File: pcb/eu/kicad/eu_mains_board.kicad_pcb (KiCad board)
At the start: 2 copper layers, 57.9 x 57.9 mm, 10 parts, among them J1 2604-3102, J2 2604-3102, J3 TSM-102-01-L-SV

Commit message: Boards for v0.4: ring board, mic carrier, riser, cover flex, EU cap board, wiring board posts
- Ring board, mic carrier and riser in pcb/sensor/ (D-50, D-60, D-68); carrier and riser fab
  packs; the ring board waits on the MSR-2's CN2 part and map
- Riser 14 x 12 mm, pins above and between the posts; cover flex with the run past the GND
  contact post and a jog from the pad section (D-79)
- EU cap board on the carrier, closed snap windows, wider with the face plate (D-56, D-70,
  D-77, D-78); EU 5 V board pins follow the back cover's pads
- Wiring board: WA-SMSI spacer posts in the 5 V area (SMT, spigot inside the board), J2
- ERC / DRC clean on every board
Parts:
- J3: value TSM-102-01-L-SV -> TSM-102-02-L-SV
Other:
- board text added: "J3 Samtec TSM-102-02-L-SV"
- board text removed: "J3 Samtec TSM-102-01-L-SV"

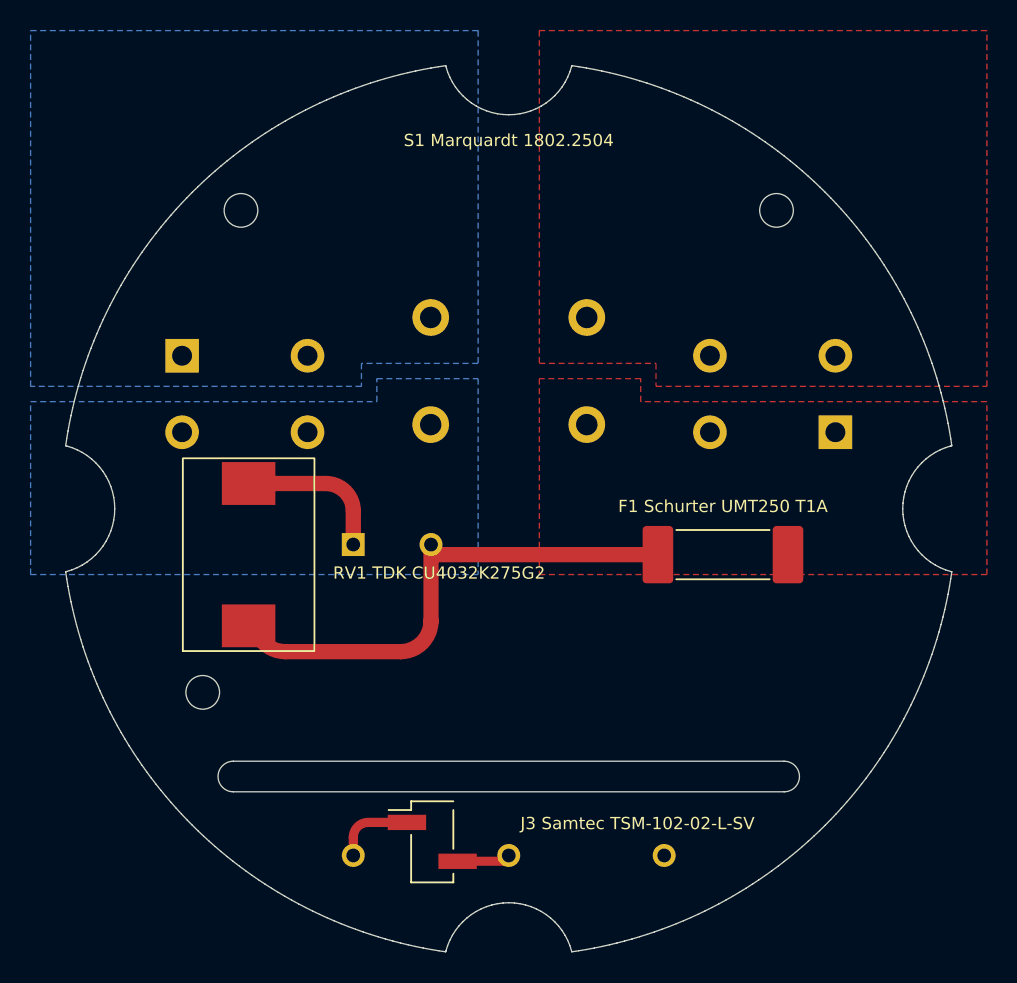
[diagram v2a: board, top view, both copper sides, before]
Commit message: Mic on the boards, parts audit, rocker second source, CN2 land pattern, back cover fit (D-82..D-90)
- Prototype PCBWay packs for the ring board, EU cap board and cover flex; logos and URL on the
  boards with room for them
- CN2 mate: Molex 55909-2474 on an assumed 51338-2474 (D-82); land pattern from Molex
  SD-55909-003 rev J, B2B from SD-51338-003 rev K (D-89); contact map and pin 1 still open
- Microphone: Knowles SPK0641HT4H-1 + ADAU7002 on the ring board and the EU cap board, the mic
  carrier removed; face plate sound column on a gasket (D-83); C3 KEMET C1206C104J3GACTU C0G
  (D-85)
- Parts rule (active, stocked at DigiKey or Mouser) and audit: F1 3403.0166.11, cover flex 1 uF
  CL05A105KO5NNNC, rocker at Mouser 979-1802.2504 (D-84)
- Rocker: tabs soldered into plated slots accepted (D-86); E-Switch RA412C1100 second source,
  slotted footprint on the wiring board and the EU mains board, solder the rocker after the
  board is screwed down (D-88)
- Back cover: round-over 8.1 x 8.0 from the printed gauges (D-87); four tabs inside the long
  side walls into the housing's slots (D-90); back_gauges_PLA
- make stock / make order-push (pcb/tools/distributors.py): live DigiKey / Mouser stock and
  lifecycle, DigiKey myLists link and Mouser cart; keys from the environment only
- Boards ERC / DRC clean; make check, make eu, make check-renders pass; renders, fab and
  order packs regenerated
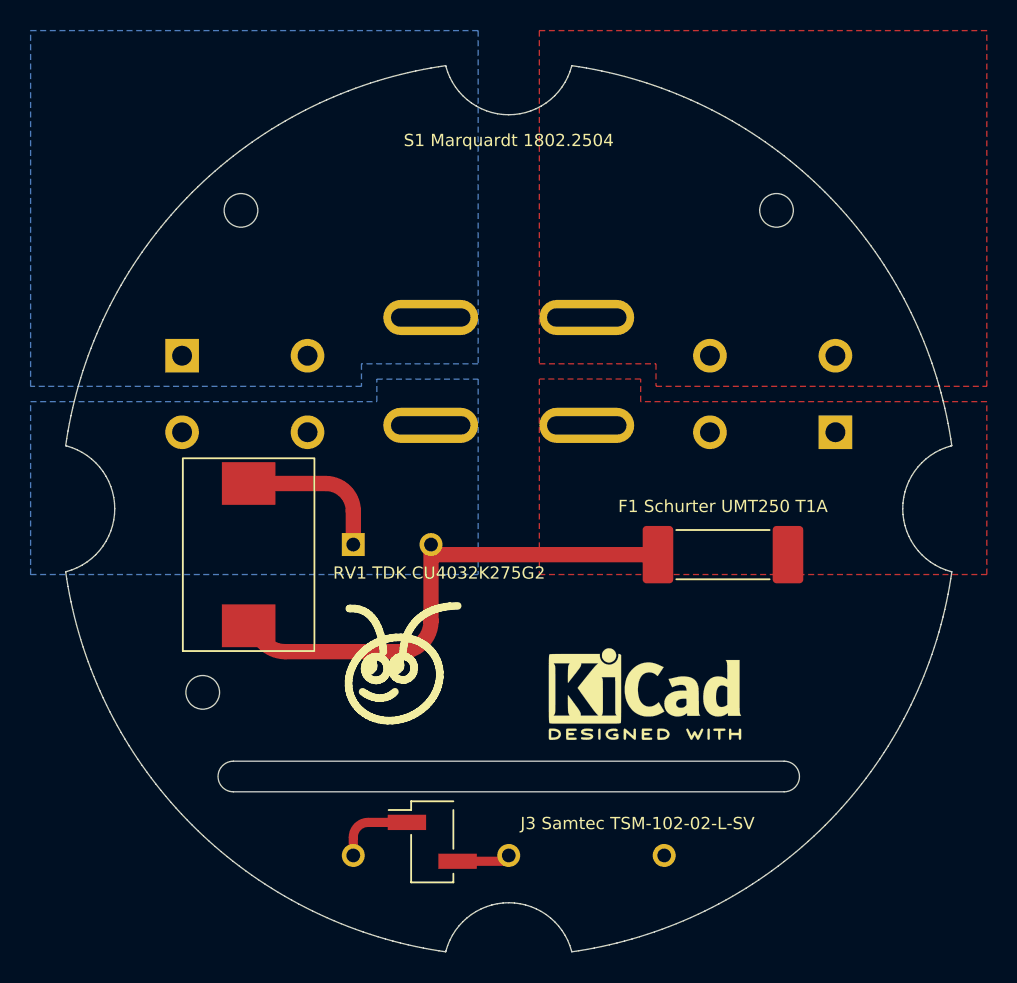
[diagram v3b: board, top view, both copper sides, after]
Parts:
- added LOGO1: Ant_Logo_8mm_SilkScreen, eu:Ant_Logo_8mm_SilkScreen, F.Cu at (93.1, 110.1)
- added LOGO2: KiCad-Logo2_5mm_SilkScreen, eu:KiCad-Logo2_5mm_SilkScreen, F.Cu at (108.9, 112.1)
- S1: footprint eu:Marquardt_1802.2504_DPST_PCB -> eu:Rocker_DPST_Marquardt_1802.2504_E-Switch_RA412C1100
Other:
- board text added: "github.com/antevens/smart-wallplate"

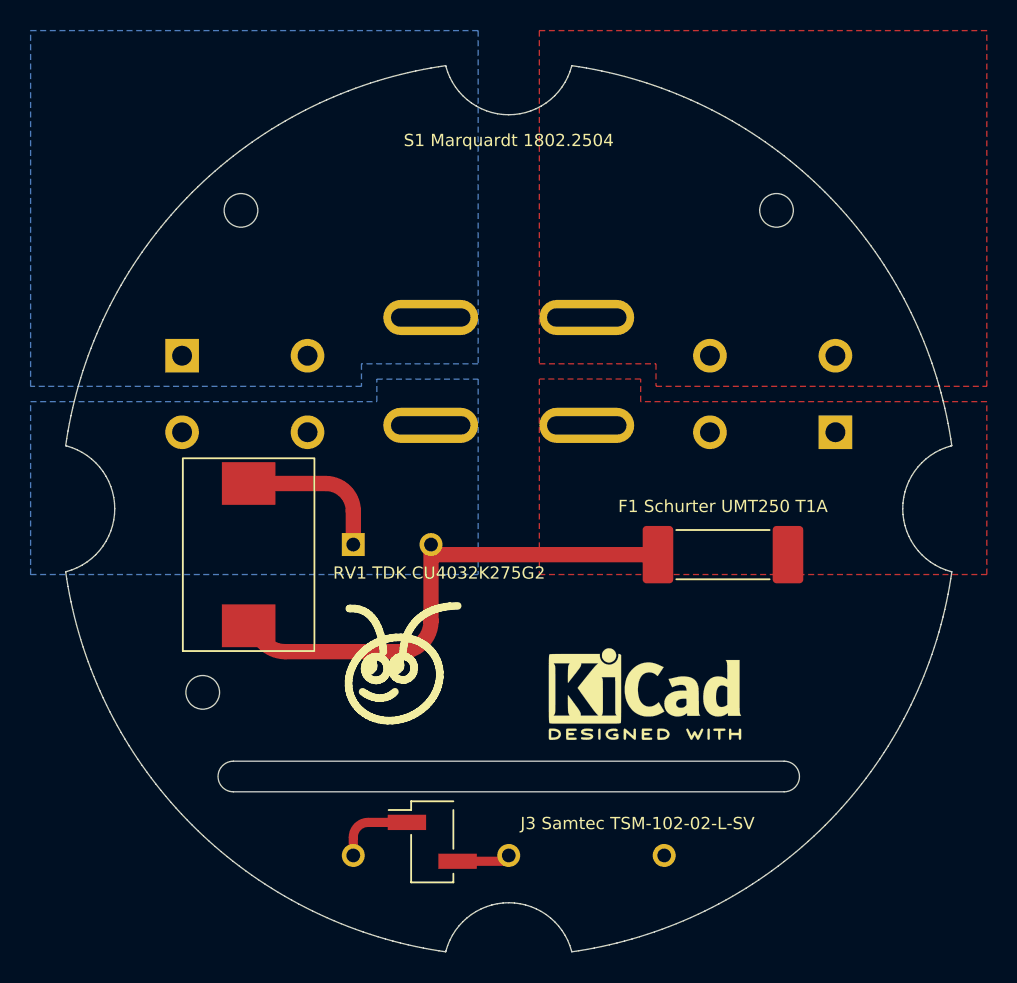
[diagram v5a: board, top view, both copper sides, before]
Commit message: EU PSU: Zettler ZPI03S0500WC instead of the Traco TMPS 03-105 (D-100)
- 8.72 against 24.09 CAD at DigiKey (an EU plate's parts 63.54, was 78.91); 5 V 600 mA,
  I/P-O/P 3600 VAC, UL/EN 62368-1; body 25 x 25 x 16 +-0.5 (PSU the maximum)
- Footprint from Zettler's PCB layout (AC pins 15 apart, outputs 5 apart, rows 15 apart, 1.2
  holes), 4-pin symbol; the NC pin and its DRC rule removed
- Mains board re-laid: fused line track 3.5 from the N pin, relief slot y -15, 5 V header x 8.5
  beside V+, F1 (15.0, -2.5), front logos above the slot; both EU boards ERC / DRC clean,
  make eu passes
- Open for review: reinforced insulation and overvoltage category not stated; Zettler's input
  fuse 0.5 A (F1 is T1A); DigiKey stock 142
- Order lists, PCBWay packs and renders regenerated
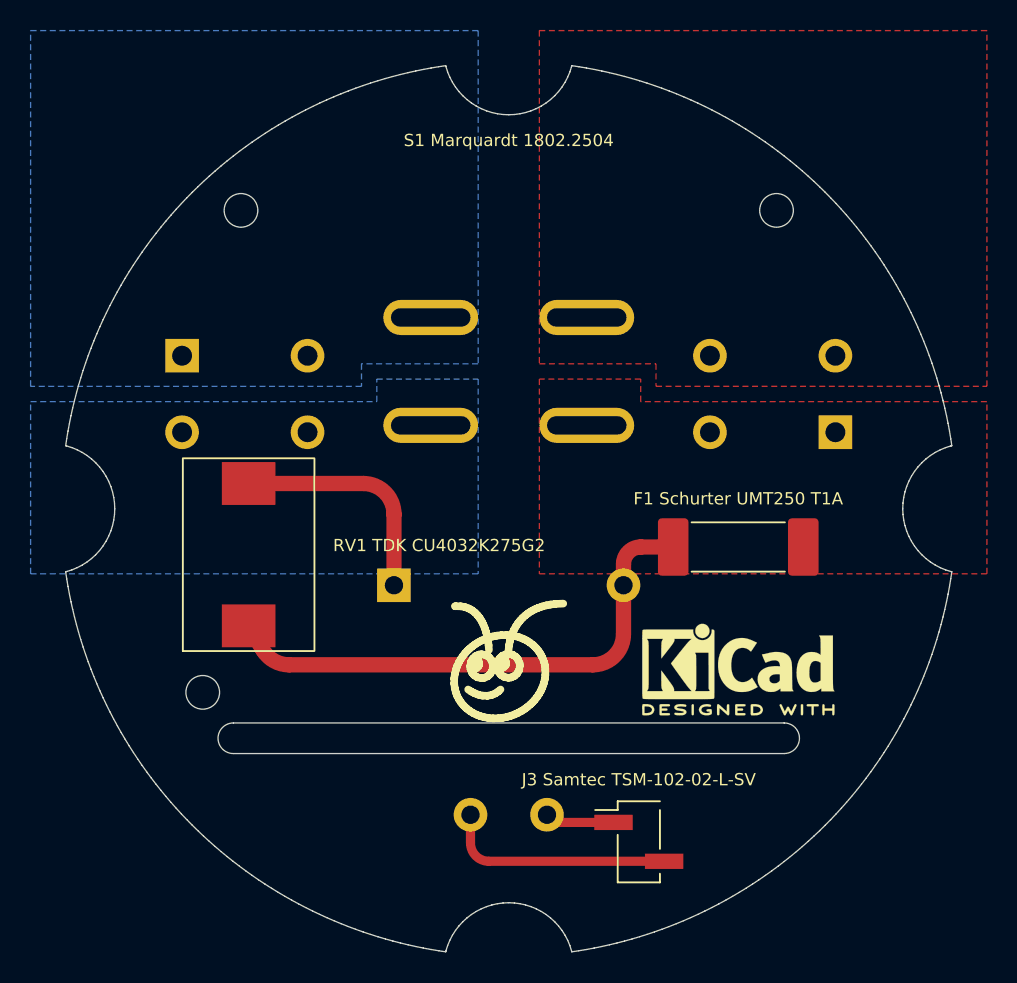
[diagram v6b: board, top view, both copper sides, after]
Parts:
- PS1: value TMPS 03-105 -> ZPI03S0500WC; footprint eu:Converter_ACDC_TRACO_TMPS03_THT -> eu:Converter_ACDC_Zettler_ZPI03_THT
- moved J3 13.5 mm to (108.5, 121.8)
- moved LOGO1 6.90 mm to (100.0, 110.0)
- moved LOGO2 6.31 mm to (115.0, 110.5)
- moved F1 1.12 mm to (115.0, 102.5)
- turned PS1 to 0 degrees
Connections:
- PS1 pad 3: unconnected-(PS1-NC-Pad3) -> +5V
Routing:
- net GND: track 3.64 -> 15.1 mm
- net /N_SW: track 9.99 -> 15.2 mm
- net /L_F: track 34.0 -> 35.2 mm
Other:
- outline, holes or cut-outs redrawn
- board text added: "PS1 Zettler Magnetics ZPI03S0500WC"
- board text removed: "PS1 Traco Power TMPS 03-105"

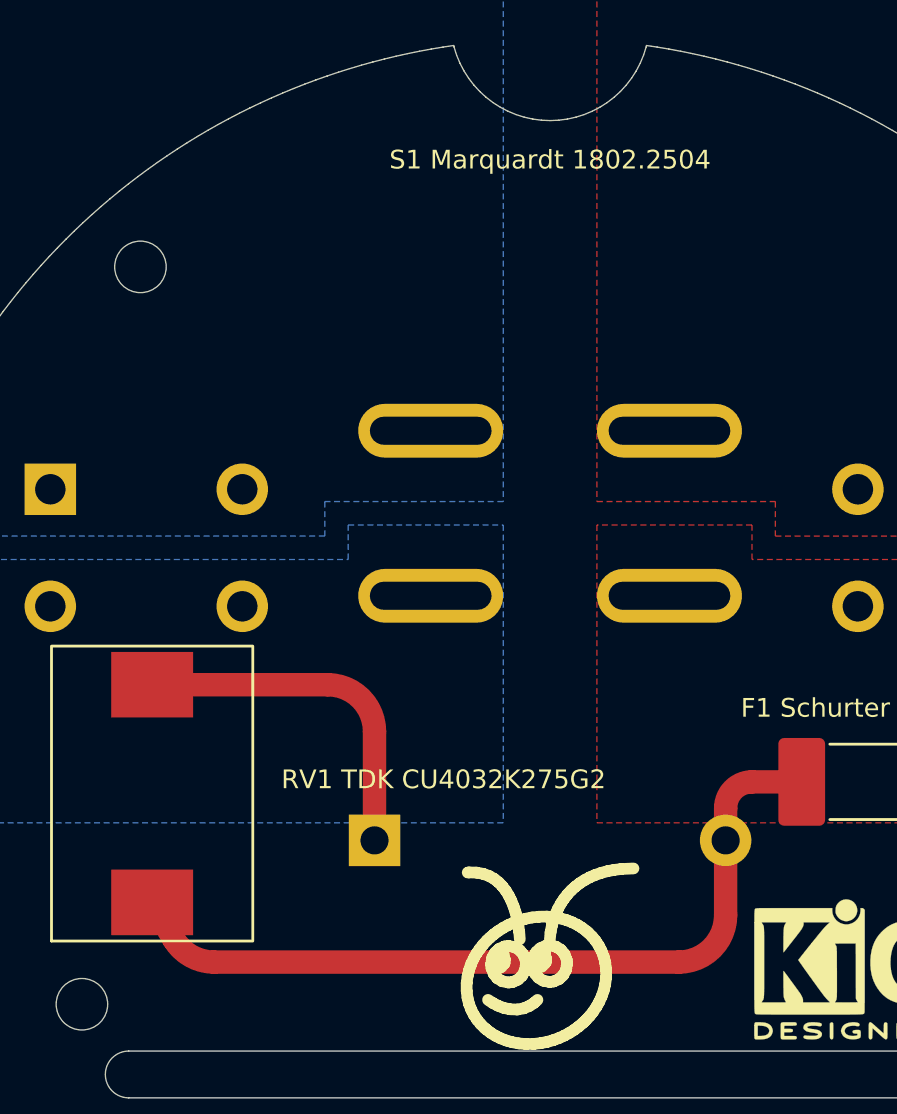
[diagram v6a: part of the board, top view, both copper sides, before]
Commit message: v0.5: back cover ends, mains spacing 3.0 mm, NA fuse separation, labels, bare renders (D-101..D-106)
- D-101: back cover shell gauges (R15..R20.9); the stadium end is confirmed
- D-102: mains spacing 3.0 mm on high-CTI FR4 (MAINS_GAP, NA and EU)
- D-103: back cover end walls 1.40 mm, inside 0.2 mm longer (BC_END_WALL)
- D-104: NA wiring board: any two mains nets 3.0 mm apart, L_F re-routed
  F1.2 -> RV1.1, L_SW vias below F1, L_SW pour up towards the rocker;
  EU mains board checked, unchanged
- D-105: rocker silkscreen "E-Switch RA412C1100 or Marquardt 1802.2504",
  EU 5 V socket part on its label; bare 3D renders for every board
- D-106: version v0.5; v0.4 fab packs, PCBWay packs and renders removed
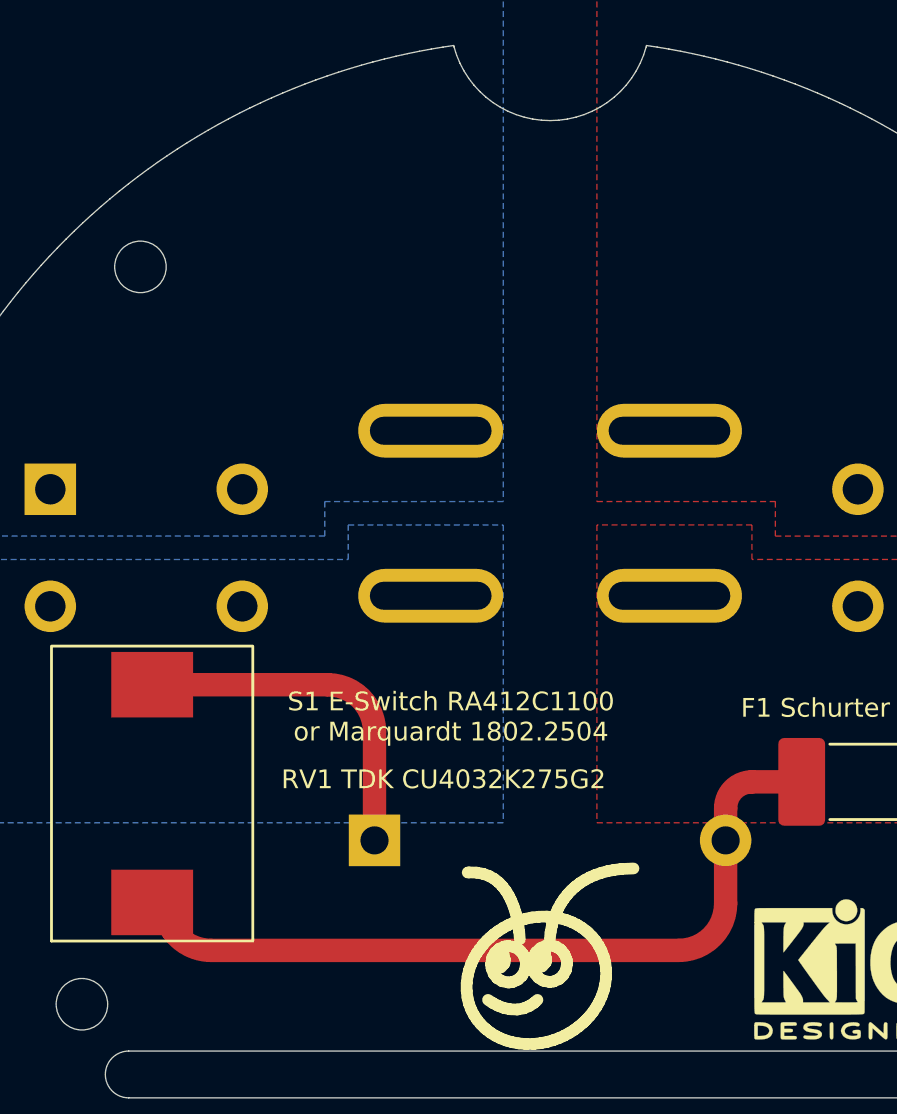
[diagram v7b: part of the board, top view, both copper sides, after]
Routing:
- net /L_F: track 35.2 -> 34.4 mm
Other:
- board text added: "S1 E-Switch RA412C1100 or Marquardt 1802.2504"
- board text removed: "S1 Marquardt 1802.2504"
